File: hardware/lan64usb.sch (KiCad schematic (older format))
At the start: 0 parts

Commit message: Angefangen den Schaltplan in KiCAD zu zeichnen.
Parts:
- added C? (x2): C, symbol C
- added R?: 10k, symbol R
- added U?: ATMEGA8-16AU, TQFP32, symbol ATMEGA8-16AU
- added Y?: Crystal 12MHz, symbol Crystal
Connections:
- new net: C?.1, U?.7 (PB6(XTAL1/TOSC1)), Y?.1
- new net: C?.1, U?.8 (PB7(XTAL2/TOSC2)), Y?.2
- new net +5V: R?.2, U?.18 (AVCC), U?.20 (AREF), U?.4 (VCC), U?.6 (VCC)
- new net GND: C?.2, C?.2, U?.21 (AGND), U?.3 (GND), U?.5 (GND)
- new net RESET: R?.1, U?.29 (PC6(~RESET~))
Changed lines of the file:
@@
 Comment4 ""
 $EndDescr
+$Comp
+L ATMEGA8-16AU U?
+U 1 1 5AFB2BDA
+P 5800 3500
+F 0 "U?" H 5050 4700 50  0000 L BNN
+F 1 "ATMEGA8-16AU" H 6300 1950 50  0000 L BNN
+F 2 "TQFP32" H 5800 3500 50  0001 C CIN
+F 3 "" H 5800 3500 50  0001 C CNN
+	1    5800 3500
+	1    0    0    -1
+$EndComp
+$Comp
+L +5V #PWR?
+U 1 1 5AFB2F75
+P 5800 2000
+F 0 "#PWR?" H 5800 1850 50  0001 C CNN
+F 1 "+5V" H 5800 2140 50  0000 C CNN
+F 2 "" H 5800 2000 50  0001 C CNN
+F 3 "" H 5800 2000 50  0001 C CNN
+	1    5800 2000
+	1    0    0    -1
+$EndComp
+$Comp
+L GND #PWR?
+U 1 1 5AFB2FA5
+P 5800 5250
+F 0 "#PWR?" H 5800 5000 50  0001 C CNN
+F 1 "GND" H 5800 5100 50  0000 C CNN
+F 2 "" H 5800 5250 50  0001 C CNN
+F 3 "" H 5800 5250 50  0001 C CNN
+	1    5800 5250
+	1    0    0    -1
+$EndComp
+$Comp
+L R R?
+U 1 1 5AFB3024
+P 4200 2500
+F 0 "R?" V 4280 2500 50  0000 C CNN
+F 1 "10k" V 4200 2500 50  0000 C CNN
+F 2 "" V 4130 2500 50  0001 C CNN
+F 3 "" H 4200 2500 50  0001 C CNN
+	1    4200 2500
+	0    1    1    0
+$EndComp
+$Comp
+L +5V #PWR?
+U 1 1 5AFB30E3
+P 3700 2500
+F 0 "#PWR?" H 3700 2350 50  0001 C CNN
+F 1 "+5V" H 3700 2640 50  0000 C CNN
+F 2 "" H 3700 2500 50  0001 C CNN
+F 3 "" H 3700 2500 50  0001 C CNN
+	1    3700 2500
+	0    -1   -1   0
+$EndComp
+Text Label 4450 2500 0    60   ~ 0
+RESET
+$Comp
+L GND #PWR?
+U 1 1 5AFB32BD
+P 3650 2900
+F 0 "#PWR?" H 3650 2650 50  0001 C CNN
+F 1 "GND" H 3650 2750 50  0000 C CNN
+F 2 "" H 3650 2900 50  0001 C CNN
+F 3 "" H 3650 2900 50  0001 C CNN
+	1    3650 2900
+	0    1    1    0
+$EndComp
+$Comp
+L Crystal Y?
+U 1 1 5AFB335E
+P 4400 3300
+F 0 "Y?" H 4400 3450 50  0000 C CNN
+F 1 "Crystal 12MHz" V 4150 3400 50  0000 C CNN
+F 2 "" H 4400 3300 50  0001 C CNN
+F 3 "" H 4400 3300 50  0001 C CNN
+	1    4400 3300
+	0    1    1    0
+$EndComp
+Wire Wire Line
+	5750 2200 5750 2000
+Wire Wire Line
+	5750 2000 5800 2000
+Wire Wire Line
+	5800 2000 5850 2000
+Wire Wire Line
+	5850 2000 5850 2200
+Connection ~ 5800 2000
+Wire Wire Line
+	5750 5100 5750 5250
+Wire Wire Line
+	5750 5250 5800 5250
+Wire Wire Line
+	5800 5250 5850 5250
+Wire Wire Line
+	5850 5250 5850 5100
+Connection ~ 5800 5250
+Wire Wire Line
+	3700 2500 3850 2500
+Wire Wire Line
+	3850 2500 4050 2500
+Wire Wire Line
+	4350 2500 4900 2500
+Wire Wire Line
+	4900 2700 3850 2700
+Wire Wire Line
+	3850 2500 3850 2700
+Wire Wire Line
+	3850 2700 3850 2800
+Connection ~ 3850 2500
+Wire Wire Line
+	3850 2800 4900 2800
+Connection ~ 3850 2700
+Wire Wire Line
+	3650 2900 4900 2900
+Wire Wire Line
+	4900 3200 4750 3200
+Wire Wire Line
+	4750 3200 4750 3100
+Wire Wire Line
+	4750 3100 4400 3100
+Wire Wire Line
+	4400 3100 4150 3100
+Wire Wire Line
+	4400 3100 4400 3150
+Wire Wire Line
+	4400 3450 4400 3500
+Wire Wire Line
+	4150 3500 4400 3500
+Wire Wire Line
+	4400 3500 4750 3500
+Wire Wire Line
+	4750 3500 4750 3400
+Wire Wire Line
+	4750 3400 4900 3400
+$Comp
+L C C?
+U 1 1 5AFB356E
+P 4000 3100
+F 0 "C?" H 4025 3200 50  0000 L CNN
+F 1 "C" H 4025 3000 50  0000 L CNN
+F 2 "" H 4038 2950 50  0001 C CNN
+F 3 "" H 4000 3100 50  0001 C CNN
+	1    4000 3100
+	0    1    1    0
+$EndComp
+$Comp
+L C C?
+U 1 1 5AFB35E5
+P 4000 3500
+F 0 "C?" H 4025 3600 50  0000 L CNN
+F 1 "C" H 4025 3400 50  0000 L CNN
+F 2 "" H 4038 3350 50  0001 C CNN
+F 3 "" H 4000 3500 50  0001 C CNN
+	1    4000 3500
+	0    1    1    0
+$EndComp
+Connection ~ 4400 3100
+Connection ~ 4400 3500
+Wire Wire Line
+	3850 3100 3750 3100
+Wire Wire Line
+	3750 3100 3750 3300
+Wire Wire Line
+	3750 3300 3750 3500
+Wire Wire Line
+	3750 3500 3850 3500
+$Comp
+L GND #PWR?
+U 1 1 5AFB36A7
+P 3650 3300
+F 0 "#PWR?" H 3650 3050 50  0001 C CNN
+F 1 "GND" H 3650 3150 50  0000 C CNN
+F 2 "" H 3650 3300 50  0001 C CNN
+F 3 "" H 3650 3300 50  0001 C CNN
+	1    3650 3300
+	0    1    1    0
+$EndComp
+Wire Wire Line
+	3650 3300 3750 3300
+Connection ~ 3750 3300
 $EndSCHEMATC

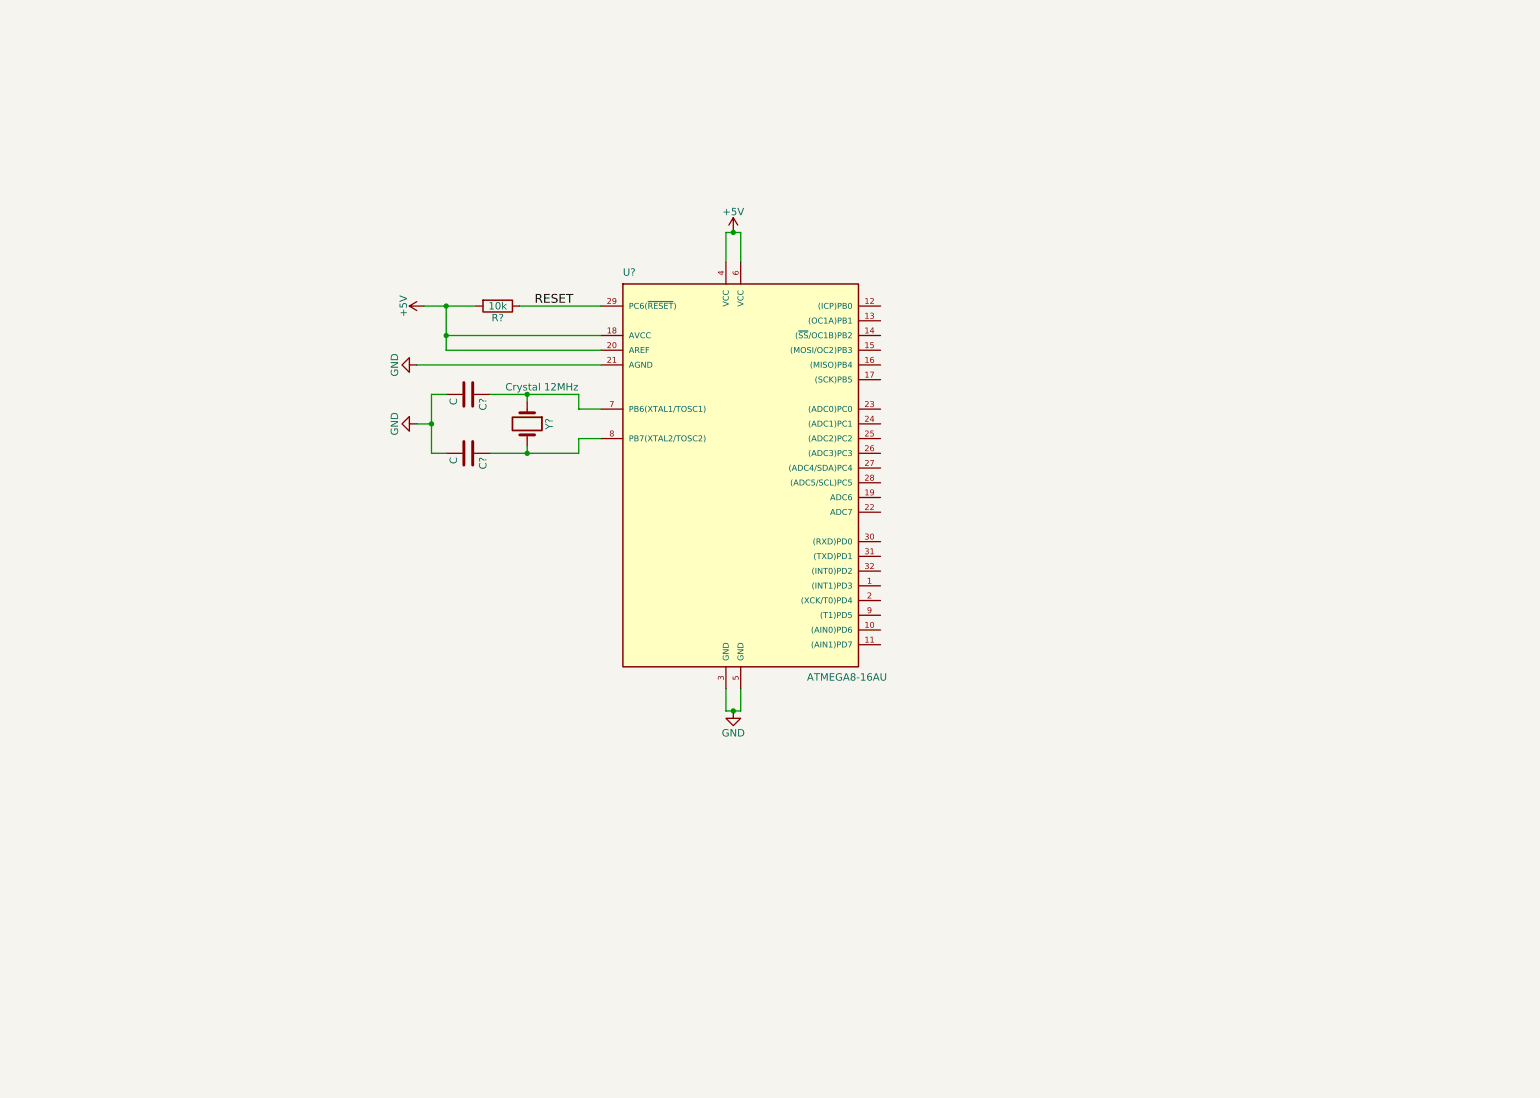
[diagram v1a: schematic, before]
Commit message: Schaltplan in KiCad fertig gezeichnet. Rev auf 1.1.0 gesetzt.
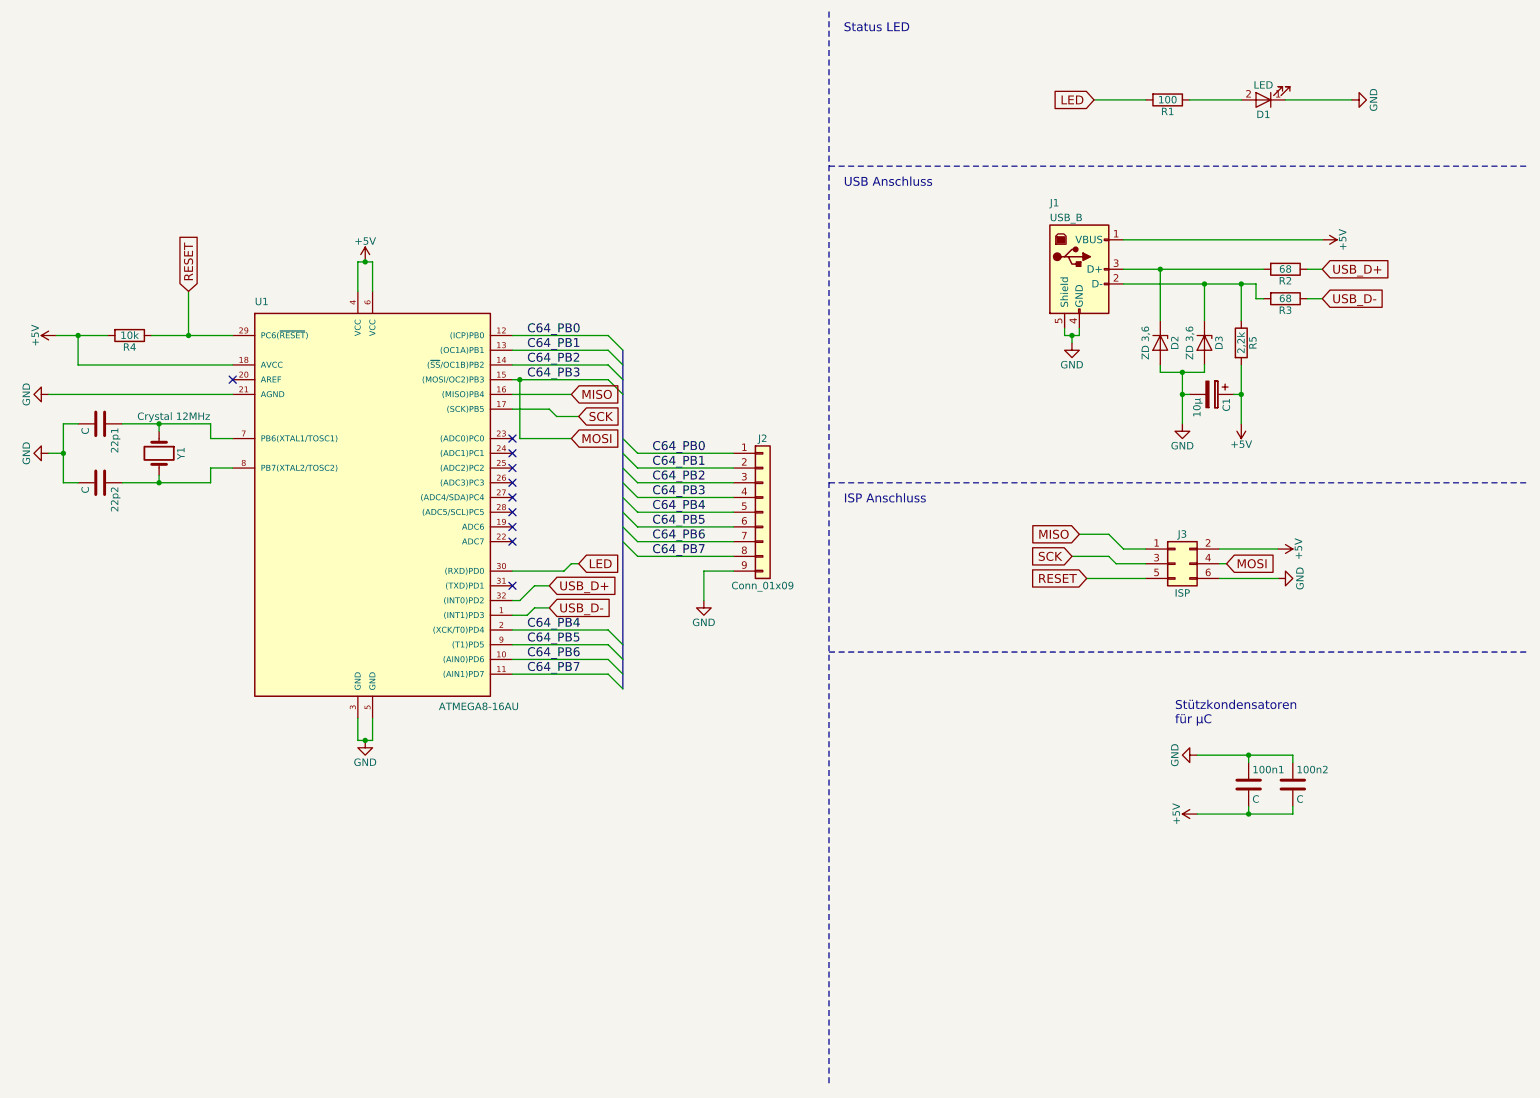
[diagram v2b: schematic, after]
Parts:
- added 100n1, 100n2: C, symbol C
- added C1: 10µ, symbol CP
- added D1: LED, symbol LED
- added D2, D3: ZD 3,6, symbol D_Zener
- added J1: USB_B, symbol USB_B
- added J2: Conn_01x09, symbol Conn_01x09
- added J3: ISP, symbol Conn_02x03_Odd_Even
- added R1: 100, symbol R
- added R2, R3: 68, symbol R
- added R5: 2,2k, symbol R
- gave numbers to parts that had none: 5
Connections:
- net +5V: now also 100n1.2, 100n2.2, C1.1, J1.1 (VBUS), J3.2 (Pin_2), R5.2; no longer U1.20 (AREF)
- net GND: now also 100n1.1, 100n2.1, C1.2, D1.1 (K), D2.2 (A), D3.2 (A), J1.4 (GND), J1.5 (Shield), J2.9 (Pin_9), J3.6 (Pin_6)
- net RESET: now also J3.5 (Pin_5)
- net USB_D-: now reaches U1.1 ((INT1)PD3)
- net USB_D-: now also R3.1
- net C64_PB6: now reaches U1.10 ((AIN0)PD6)
- net C64_PB6: now also J2.7 (Pin_7)
- net C64_PB7: now reaches U1.11 ((AIN1)PD7)
- net C64_PB7: now also J2.8 (Pin_8)
- net C64_PB0: now reaches U1.12 ((ICP)PB0)
- net C64_PB0: now also J2.1 (Pin_1)
- net C64_PB1: now reaches U1.13 ((OC1A)PB1)
- net C64_PB1: now also J2.2 (Pin_2)
- net C64_PB2: now reaches U1.14 ((~SS~/OC1B)PB2)
- net C64_PB2: now also J2.3 (Pin_3)
- net MOSI: now reaches U1.15 ((MOSI/OC2)PB3)
- net MOSI: now also J2.4 (Pin_4), J3.4 (Pin_4)
- net MISO: now reaches U1.16 ((MISO)PB4)
- net MISO: now also J3.1 (Pin_1)
- net SCK: now reaches U1.17 ((SCK)PB5)
- net SCK: now also J3.3 (Pin_3)
- net C64_PB4: now reaches U1.2 ((XCK/T0)PD4)
- net C64_PB4: now also J2.5 (Pin_5)
- net LED: now reaches U1.30 ((RXD)PD0)
- net LED: now also R1.2
- net USB_D+: now reaches U1.32 ((INT0)PD2)
- net USB_D+: now also R2.1
- net C64_PB5: now reaches U1.9 ((T1)PD5)
- net C64_PB5: now also J2.6 (Pin_6)
- new net: D1.2 (A), R1.1
- new net: D3.1 (K), J1.2 (D-), R3.2, R5.1
- new net: D2.1 (K), J1.3 (D+), R2.2
- no-connect marks 0 -> 10
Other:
- note added: "ISP Anschluss"
- note added: "Status LED"
- note added: "Stützkondensatoren\nfür µC\n"
- note added: "USB Anschluss"
- moved on the sheet: 22p1, 22p2, R4, U1, Y1

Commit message: Schaltplan für DIP Bauteile angepasst. Rev.: 1.2.0
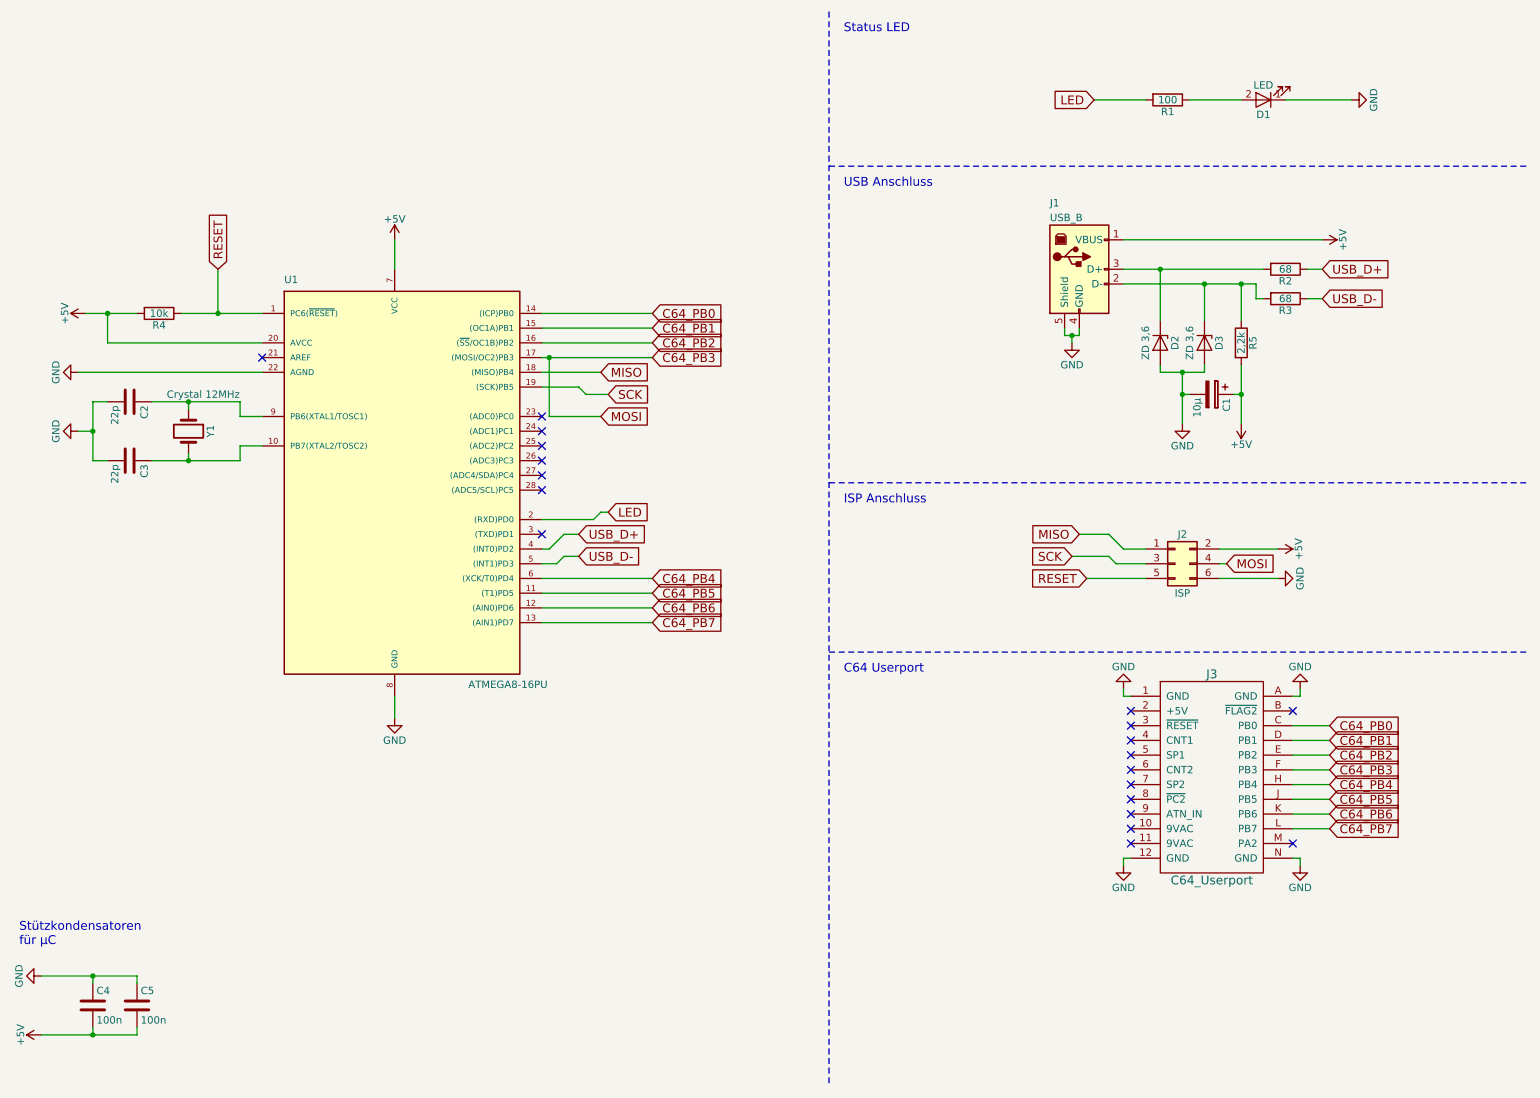
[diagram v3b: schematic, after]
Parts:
- removed J2: Conn_01x09, symbol Conn_01x09
- removed U1: ATMEGA8-16AU, TQFP32, symbol ATMEGA8-16AU
- added J3: C64_Userport, symbol C64_Userport
- added U1: ATMEGA8-16PU, DIL28, symbol ATMEGA8-16PU
- C2: renamed from 22p1; value C -> 22p
- C3: renamed from 22p2; value C -> 22p
- C4: renamed from 100n1; value C -> 100n
- C5: renamed from 100n2; value C -> 100n
- renumbered J3 to J2
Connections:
- net +5V: now also U1.20 (AVCC), U1.7 (VCC)
- net C64_PB0: now also J3.C (PB0), U1.14 ((ICP)PB0)
- net C64_PB1: now also J3.D (PB1), U1.15 ((OC1A)PB1)
- net C64_PB2: now also J3.E (PB2), U1.16 ((~SS~/OC1B)PB2)
- net C64_PB4: now also J3.H (PB4), U1.6 ((XCK/T0)PD4)
- net C64_PB5: now also J3.J (PB5), U1.11 ((T1)PD5)
- net C64_PB6: now also J3.K (PB6), U1.12 ((AIN0)PD6)
- net C64_PB7: now also J3.L (PB7), U1.13 ((AIN1)PD7)
- net GND: now also J3.1 (GND), J3.12 (GND), J3.A (GND), J3.N (GND), U1.22 (AGND), U1.8 (GND)
- net LED: now also U1.2 ((RXD)PD0)
- net MISO: now also U1.18 ((MISO)PB4)
- net RESET: now also U1.1 (PC6(~RESET~))
- net SCK: now also U1.19 ((SCK)PB5)
- net USB_D+: now also U1.4 ((INT0)PD2)
- net USB_D-: now also U1.5 ((INT1)PD3)
- net at C2.1, Y1.1: now also U1.9 (PB6(XTAL1/TOSC1))
- net at C3.1, Y1.2: now also U1.10 (PB7(XTAL2/TOSC2))
- net MOSI renamed C64_PB3
- net C64_PB3: now also J3.F (PB3), U1.17 ((MOSI/OC2)PB3)
- no-connect marks 10 -> 20
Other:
- note added: "C64 Userport"
- moved on the sheet: C2, C3, C4, C5, R4, Y1
